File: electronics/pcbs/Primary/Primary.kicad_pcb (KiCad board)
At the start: 2 copper layers, 102 x 53.3 mm, 26 parts, among them J1 Line Sensor 1, J11 I2C Bus, J12 Battery, J13 Pololu_D24V50F5, J14 Magnet, J2 Line Sensor 2, J3 Line Sensor 3, J4 Line Sensor 4, J5 Line Sensor 5, J6 Line Sensor 6, J7 Servo, J8 Pololu_DRV8834, J9 Stepper Motor, P1 Digital, P10 CONN_01X01, P11 CONN_01X01, P12 CONN_01X01, P13 CONN_01X01, P2 Power, P3 Analog, P4 Analog, P5 PWM, P6 PWM, P7 Communication, P8 CONN_01X01, P9 CONN_01X01

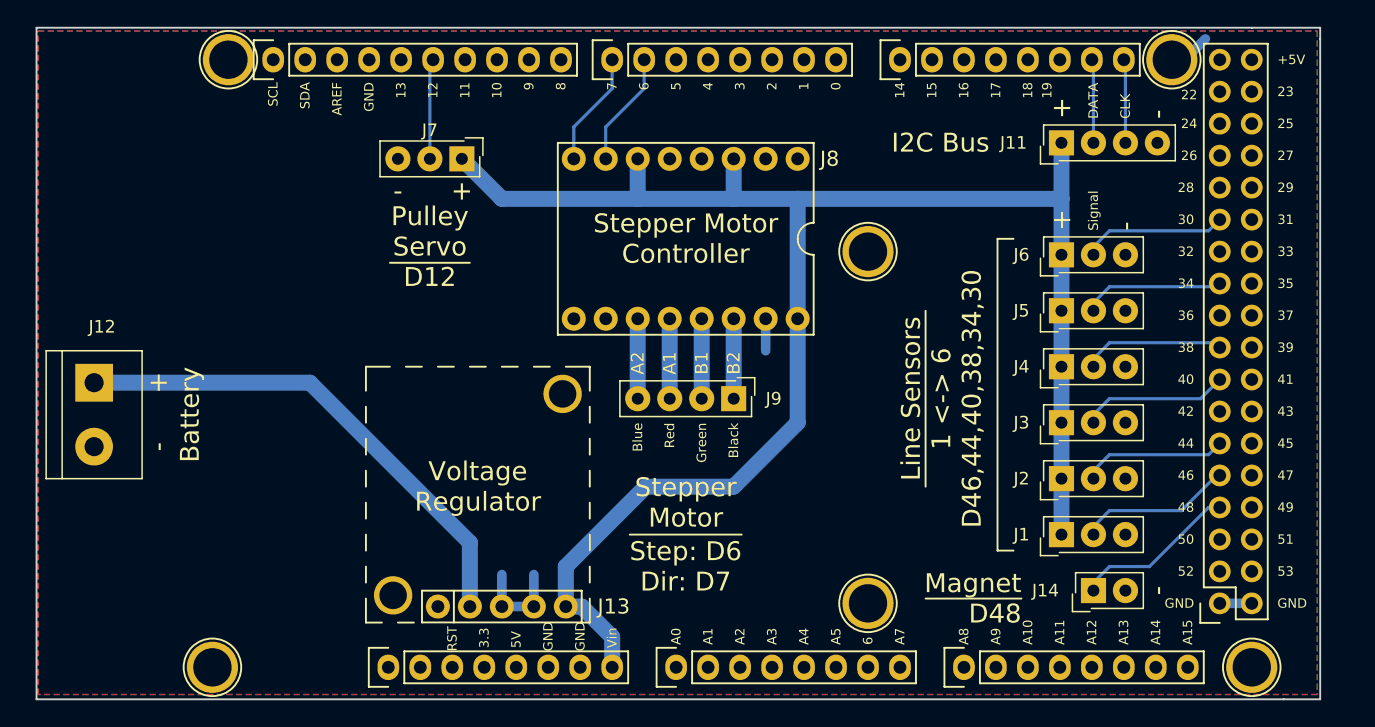
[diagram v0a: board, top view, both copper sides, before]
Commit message: Primary PCB: Power the Arduino with VBATT rather than Regulated 5V.
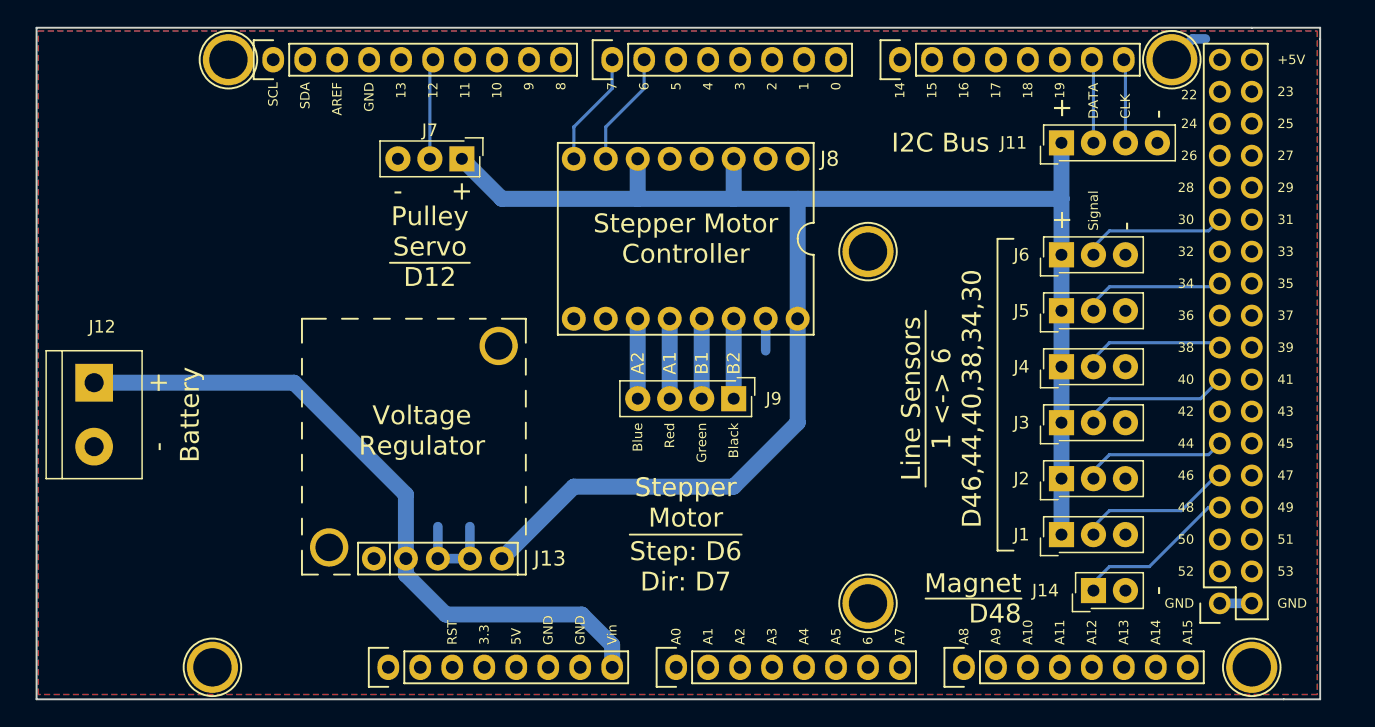
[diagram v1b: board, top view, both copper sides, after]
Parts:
- moved J13 6.35 mm to (130.2, 110.5)
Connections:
- P2 pad 8: +5V -> +BATT
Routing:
- net +BATT: track 40.2 -> 55.3 mm
- net +5V: track 138.9 -> 133.4 mm
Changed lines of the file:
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@@
     (links 57)
     (no_connects 2)
-    (area 96.952999 66.843 205.408601 122.995)
+    (area 103.302999 68.250999 205.408601 121.741001)
     (thickness 1.6)
     (drawings 147)
-    (tracks 84)
+    (tracks 85)
     (zones 0)
     (modules 26)
@@
       (net 1 GND))
     (pad 8 thru_hole oval (at 17.78 0) (size 1.7272 2.032) (drill 1.016) (layers *.Cu *.Mask F.SilkS)
-      (net 34 +5V))
+      (net 85 +BATT))
     (model ${KIPRJMOD}/Socket_Arduino_Mega.3dshapes/Socket_header_Arduino_1x08.wrl
       (at (xyz 0.35 0 0))
@@
   )
   (module Pololu:Pololu_D24V50F5 (layer F.Cu)
-    (at 135.255 114.3)
+    (at 130.175 110.49)
     (fp_text reference J13 (at 13.97 0) (layer F.SilkS)
       (effects (font (size 1.2 1.2) (thickness 0.15)))
@@
       (net 34 +5V))
     (pad "" thru_hole circle (at -3.556 -0.889) (size 3.048 3.048) (drill 2.1844) (layers *.Cu *.Mask)
-      (net 1 GND) (thermal_gap 0.254))
+      (net 1 GND))
     (pad "" thru_hole circle (at 9.906 -16.891) (size 3.048 3.048) (drill 2.1844) (layers *.Cu *.Mask)
-      (net 1 GND) (thermal_gap 0.254))
+      (net 1 GND))
   )
   (gr_text 22 (at 195.58 73.66) (layer F.SilkS)
@@
     (effects (font (size 0.75 0.75) (thickness 0.15)) (justify left))
   )
-  (gr_text 19 (at 183.642 72.644 90) (layer F.SilkS)
+  (gr_text 19 (at 184.658 72.644 90) (layer F.SilkS)
     (effects (font (size 0.75 0.75) (thickness 0.15)) (justify right))
   )
@@
     (effects (font (size 0.75 0.75) (thickness 0.15)) (justify left))
   )
-  (gr_text Vin (at 149.098 117.602 90) (layer F.SilkS)
-    (effects (font (size 0.75 0.75) (thickness 0.15)) (justify left))
-  )
-  (gr_text GND (at 146.558 117.856 90) (layer F.SilkS)
-    (effects (font (size 0.75 0.75) (thickness 0.15)) (justify left))
-  )
-  (gr_text GND (at 144.018 117.856 90) (layer F.SilkS)
-    (effects (font (size 0.75 0.75) (thickness 0.15)) (justify left))
-  )
-  (gr_text 5V (at 141.478 117.602 90) (layer F.SilkS)
-    (effects (font (size 0.75 0.75) (thickness 0.15)) (justify left))
-  )
-  (gr_text 3.3 (at 138.938 117.602 90) (layer F.SilkS)
+  (gr_text Vin (at 149.098 117.348 90) (layer F.SilkS)
+    (effects (font (size 0.75 0.75) (thickness 0.15)) (justify left))
+  )
+  (gr_text GND (at 146.558 117.348 90) (layer F.SilkS)
+    (effects (font (size 0.75 0.75) (thickness 0.15)) (justify left))
+  )
+  (gr_text GND (at 144.018 117.348 90) (layer F.SilkS)
+    (effects (font (size 0.75 0.75) (thickness 0.15)) (justify left))
+  )
+  (gr_text 5V (at 141.478 117.348 90) (layer F.SilkS)
+    (effects (font (size 0.75 0.75) (thickness 0.15)) (justify left))
+  )
+  (gr_text 3.3 (at 138.938 117.348 90) (layer F.SilkS)
     (effects (font (size 0.75 0.75) (thickness 0.15)) (justify left))
   )
@@
     (effects (font (size 1.5 1.5) (thickness 0.3)))
   )
-  (gr_text "Voltage\nRegulator" (at 138.43 104.775) (layer F.SilkS)
+  (gr_text "Voltage\nRegulator" (at 133.985 100.33) (layer F.SilkS)
     (effects (font (size 1.5 1.5) (thickness 0.3)))
   )
@@
   (gr_line (start 202.565 71.12) (end 202.565 81.28) (angle 90) (layer F.CrtYd) (width 0.15))
   (gr_line (start 200.025 68.58) (end 202.565 71.12) (angle 90) (layer F.CrtYd) (width 0.15))
-  (gr_text RST (at 136.398 117.856 90) (layer F.SilkS)
+  (gr_text RST (at 136.398 117.348 90) (layer F.SilkS)
     (effects (font (size 0.75 0.75) (thickness 0.15)) (justify left))
   )
@@
   (gr_line (start 103.378 68.326) (end 199.898 68.326) (angle 90) (layer Edge.Cuts) (width 0.15))
   (gr_line (start 103.378 121.666) (end 103.378 68.326) (angle 90) (layer Edge.Cuts) (width 0.15))
+  (segment (start 193.548 70.866) (end 195.199 69.215) (width 0.762) (layer B.Cu) (net 1) (status 400000))
+  (segment (start 195.199 69.215) (end 196.215 69.215) (width 0.762) (layer B.Cu) (net 1))
+  (segment (start 135.255 110.49) (end 135.255 107.95) (width 0.762) (layer B.Cu) (net 1))
+  (segment (start 137.795 110.49) (end 137.795 107.95) (width 0.762) (layer B.Cu) (net 1))
+  (segment (start 135.255 110.49) (end 137.795 110.49) (width 0.762) (layer B.Cu) (net 1))
   (segment (start 161.29 91.44) (end 161.29 93.98) (width 0.762) (layer B.Cu) (net 1))
-  (segment (start 140.335 114.3) (end 140.335 111.76) (width 0.762) (layer B.Cu) (net 1))
-  (segment (start 142.875 114.3) (end 142.875 111.76) (width 0.762) (layer B.Cu) (net 1))
-  (segment (start 140.335 114.3) (end 142.875 114.3) (width 0.762) (layer B.Cu) (net 1))
   (segment (start 197.358 114.046) (end 199.898 114.046) (width 0.762) (layer B.Cu) (net 1))
-  (segment (start 193.548 70.866) (end 194.564 70.866) (width 0.25) (layer B.Cu) (net 1))
-  (segment (start 194.564 70.866) (end 196.215 69.215) (width 0.762) (layer B.Cu) (net 1))
   (segment (start 187.325 113.03) (end 187.325 112.395) (width 0.25) (layer B.Cu) (net 6))
   (segment (start 187.325 112.395) (end 188.595 111.125) (width 0.25) (layer B.Cu) (net 6))
@@
   (segment (start 196.469 84.455) (end 197.358 83.566) (width 0.25) (layer B.Cu) (net 24))
   (segment (start 188.595 84.455) (end 196.469 84.455) (width 0.25) (layer B.Cu) (net 24))
+  (segment (start 140.335 110.49) (end 146.05 104.775) (width 1.27) (layer B.Cu) (net 34))
+  (segment (start 163.83 99.695) (end 163.83 91.44) (width 1.27) (layer B.Cu) (net 34))
+  (segment (start 158.75 104.775) (end 163.83 99.695) (width 1.27) (layer B.Cu) (net 34))
+  (segment (start 146.05 104.775) (end 158.75 104.775) (width 1.27) (layer B.Cu) (net 34))
   (segment (start 151.13 81.915) (end 140.335 81.915) (width 1.27) (layer B.Cu) (net 34))
   (segment (start 140.335 81.915) (end 137.16 78.74) (width 1.27) (layer B.Cu) (net 34))
@@
   (segment (start 158.75 81.915) (end 163.83 81.915) (width 1.27) (layer B.Cu) (net 34))
   (segment (start 163.83 81.915) (end 184.785 81.915) (width 1.27) (layer B.Cu) (net 34))
-  (segment (start 145.415 114.3) (end 145.415 111.125) (width 1.27) (layer B.Cu) (net 34))
-  (segment (start 163.83 99.695) (end 163.83 91.44) (width 1.27) (layer B.Cu) (net 34))
-  (segment (start 158.75 104.775) (end 163.83 99.695) (width 1.27) (layer B.Cu) (net 34))
-  (segment (start 151.765 104.775) (end 158.75 104.775) (width 1.27) (layer B.Cu) (net 34))
-  (segment (start 145.415 111.125) (end 151.765 104.775) (width 1.27) (layer B.Cu) (net 34))
   (segment (start 184.785 81.915) (end 184.785 77.47) (width 1.27) (layer B.Cu) (net 34) (status 10))
   (segment (start 184.785 86.36) (end 184.785 81.915) (width 1.27) (layer B.Cu) (net 34) (status 10))
@@
   (segment (start 184.785 108.585) (end 184.785 104.14) (width 1.27) (layer B.Cu) (net 34) (status 10))
   (segment (start 151.13 81.915) (end 151.13 78.74) (width 1.27) (layer B.Cu) (net 34))
-  (segment (start 145.415 114.3) (end 146.685 114.3) (width 1.27) (layer B.Cu) (net 34))
-  (segment (start 149.098 116.713) (end 149.098 119.126) (width 1.27) (layer B.Cu) (net 34))
-  (segment (start 146.685 114.3) (end 149.098 116.713) (width 1.27) (layer B.Cu) (net 34))
   (segment (start 134.62 78.74) (end 134.62 71.12) (width 0.25) (layer B.Cu) (net 57))
   (segment (start 134.62 71.12) (end 134.874 70.866) (width 0.25) (layer B.Cu) (net 57))
@@
   (segment (start 189.865 77.47) (end 189.865 70.993) (width 0.25) (layer B.Cu) (net 69))
   (segment (start 189.865 70.993) (end 189.738 70.866) (width 0.25) (layer B.Cu) (net 69))
-  (segment (start 137.795 114.3) (end 137.795 109.22) (width 1.27) (layer B.Cu) (net 85))
-  (segment (start 125.095 96.52) (end 107.95 96.52) (width 1.27) (layer B.Cu) (net 85) (status 20))
-  (segment (start 137.795 109.22) (end 125.095 96.52) (width 1.27) (layer B.Cu) (net 85))
+  (segment (start 132.715 110.49) (end 132.715 111.76) (width 1.27) (layer B.Cu) (net 85))
+  (segment (start 135.89 114.935) (end 146.685 114.935) (width 1.27) (layer B.Cu) (net 85))
+  (segment (start 146.685 114.935) (end 149.098 117.348) (width 1.27) (layer B.Cu) (net 85))
+  (segment (start 149.098 117.348) (end 149.098 119.126) (width 1.27) (layer B.Cu) (net 85))
+  (segment (start 132.715 111.76) (end 135.89 114.935) (width 1.27) (layer B.Cu) (net 85))
+  (segment (start 107.95 96.52) (end 123.825 96.52) (width 1.27) (layer B.Cu) (net 85))
+  (segment (start 132.715 105.41) (end 132.715 110.49) (width 1.27) (layer B.Cu) (net 85))
+  (segment (start 123.825 96.52) (end 132.715 105.41) (width 1.27) (layer B.Cu) (net 85))
   (segment (start 158.75 97.79) (end 158.75 91.44) (width 1.27) (layer B.Cu) (net 87))
   (segment (start 156.21 91.44) (end 156.21 97.79) (width 1.27) (layer B.Cu) (net 88))

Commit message: Primary/Motor PCBs: Rearranged the GND pin on breakout headers so that we can avoid needing two layers. This change makes the boards more easily prototyped using hobbyist tools like the OtherMill, where plating holes and vias is difficult.
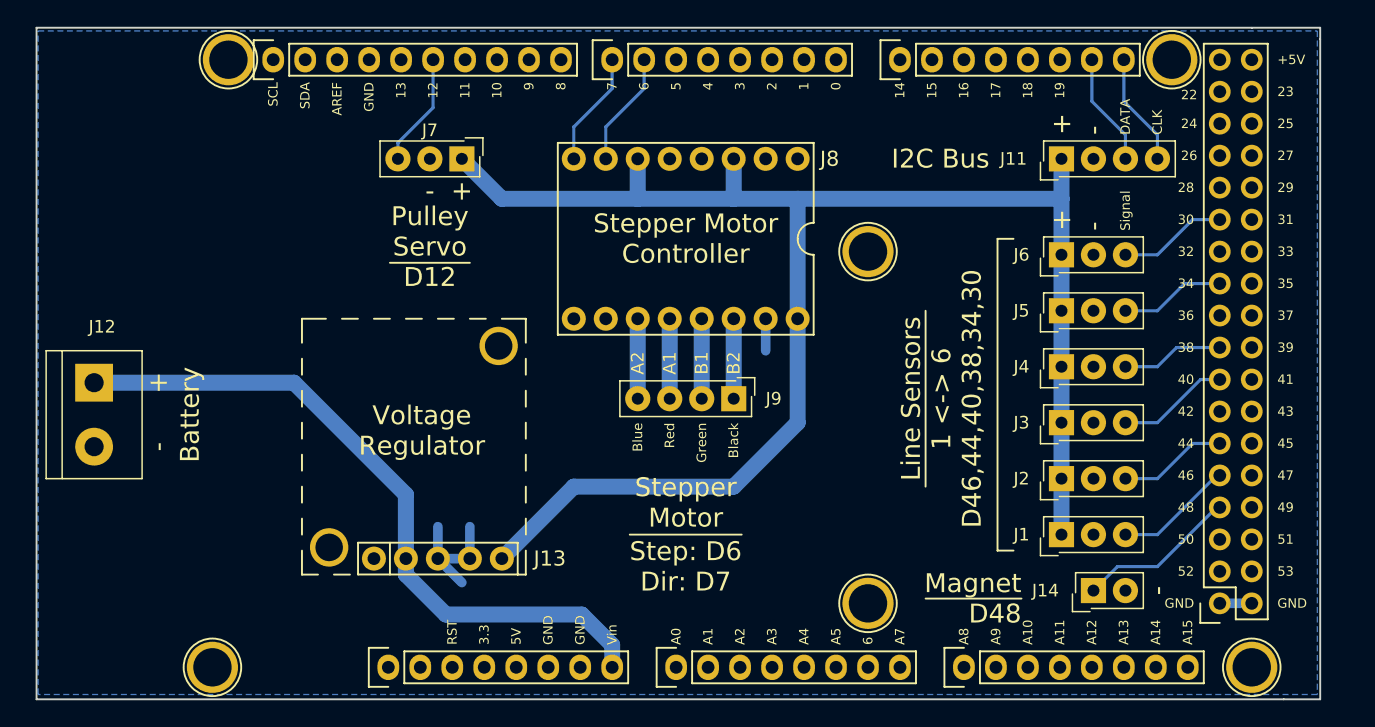
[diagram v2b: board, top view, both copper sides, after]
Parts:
- moved J11 1.27 mm to (184.8, 78.7)
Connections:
- J1 pad 2: /46 -> GND
- J1 pad 3: GND -> /46
- J11 pad 2: /20(SDA) -> GND
- J11 pad 3: /21(SCL) -> /20(SDA)
- J11 pad 4: GND -> /21(SCL)
- J2 pad 2: /44 -> GND
- J2 pad 3: GND -> /44
- J3 pad 2: /40 -> GND
- J3 pad 3: GND -> /40
- J4 pad 2: /38 -> GND
- J4 pad 3: GND -> /38
- J5 pad 2: /34 -> GND
- J5 pad 3: GND -> /34
- J6 pad 2: /30 -> GND
- J6 pad 3: GND -> /30
- J7 pad 2: /12(**) -> GND
- J7 pad 3: GND -> /12(**)
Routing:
- net /38: track 11.9 -> 8.12 mm
- net /34: track 11.7 -> 8.39 mm
- net /46: track 12.7 -> 9.44 mm
- net /44: track 11.6 -> 8.65 mm
- net /30: track 11.6 -> 8.65 mm
- net /40: track 11.8 -> 8.91 mm
- net /21(SCL): track 6.66 -> 9.16 mm
- net /20(SDA): track 6.66 -> 8.98 mm
- net +5V: track 133.4 -> 132.2 mm
- net /12(**): track 7.98 -> 9.03 mm
- net /48: track 13.5 -> 12.8 mm
- net GND: track 16.1 -> 15.4 mm
- removed copper zone on F.Cu, net GND

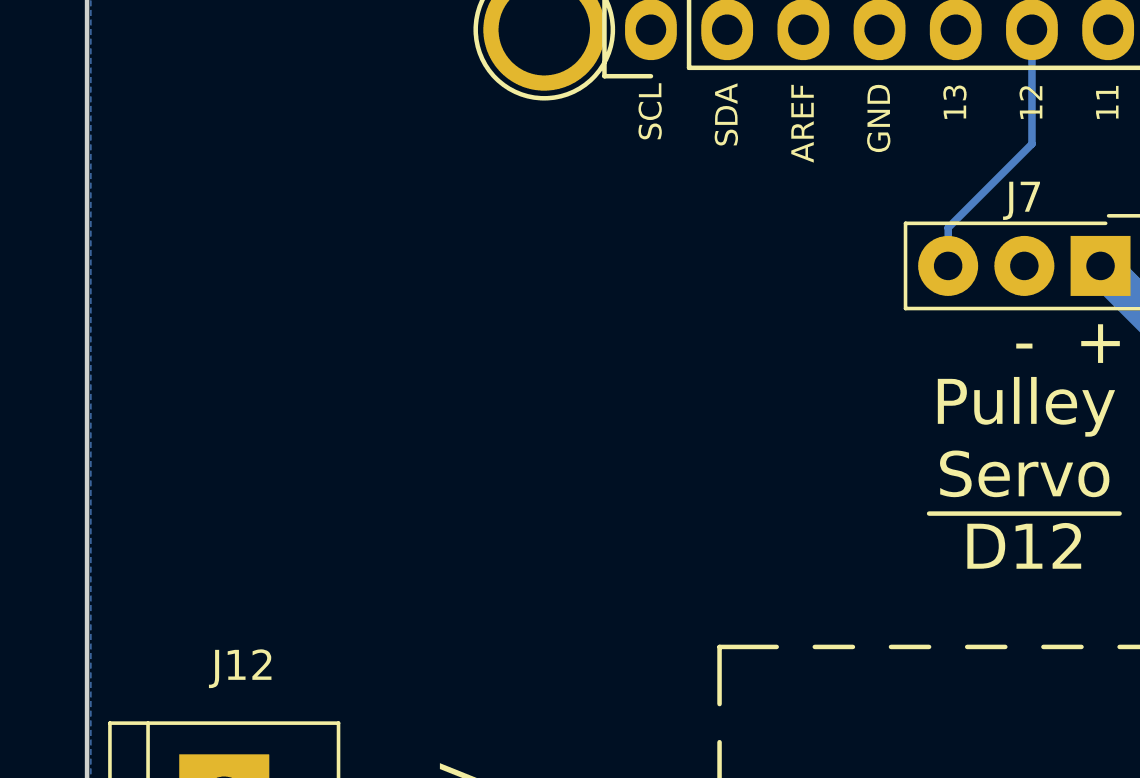
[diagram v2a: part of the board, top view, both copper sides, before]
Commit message: Primary/Motor PCBs: Added logo and competition to board silkscreens.
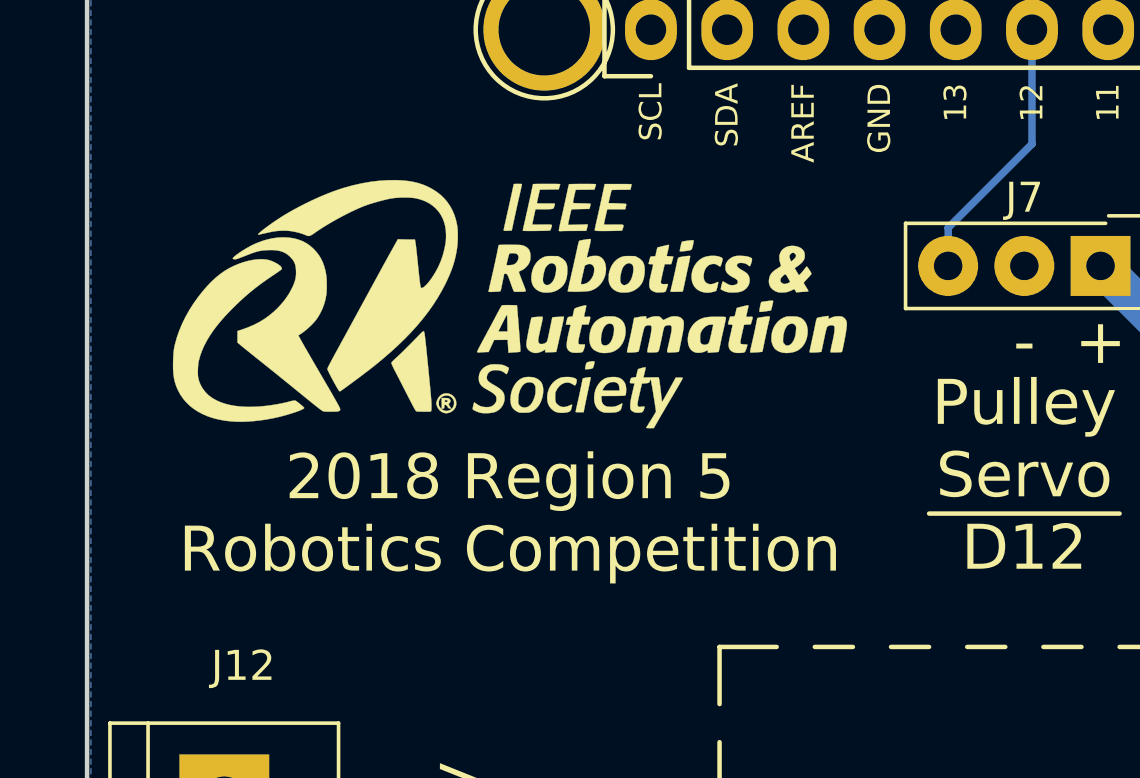
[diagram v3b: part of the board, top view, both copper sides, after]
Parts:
- added G***: LOGO, RAS:Logo, F.Cu at (117.5, 80.0)
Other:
- board text added: "2018 Region 5 Robotics Competition"
